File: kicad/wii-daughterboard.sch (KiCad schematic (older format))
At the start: 34 parts, among them J1 Data, J10 USB, J11 A/V Out, J12 Bluetooth Sync, J14 Case Panel, J2 DC In, J3 GameCube 1, J4 GameCube 2, J5 Bluetooth, J6 GameCube 3, J7 GameCube 4, J8 Motherboard Out, U1 TLV62585DRL, U2 TLV62585DRL, U3 TLV62585DRL, U4 MIC94053YC6-TR

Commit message: v2.0
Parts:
- removed J7: GameCube 4, Connector_JST:JST_SH_BM04B-SRSS-TB_1x04-1MP_P1.00mm_Vertical, symbol Connector_Generic_MountingPin:Conn_01x04_MountingPin
- removed U4: MIC94053YC6-TR, Package_TO_SOT_SMD:SOT-363_SC-70-6_Handsoldering, symbol MIC94053:MIC94053YC6-TR
- added J12: Fan Pwr, Connector_JST:JST_SH_BM02B-SRSS-TB_1x02-1MP_P1.00mm_Vertical, symbol Connector:Conn_01x02_Male
- added Q1: DMG2301L, Package_TO_SOT_SMD:SOT-23_Handsoldering, symbol Transistor_FET:DMG2301L
- added R1: 10K, Resistor_SMD:R_0603_1608Metric_Pad1.05x0.95mm_HandSolder, symbol Device:R
- added TP1: 5V, TestPoint:TestPoint_Pad_D1.0mm, symbol Connector:TestPoint
- added TP2: 3V3, TestPoint:TestPoint_Pad_D1.0mm, symbol Connector:TestPoint
- added TP3: 1V15, TestPoint:TestPoint_Pad_D1.0mm, symbol Connector:TestPoint
- added TP4: 1V0, TestPoint:TestPoint_Pad_D1.0mm, symbol Connector:TestPoint
- J10: renamed from J11; value A/V Out -> A/V Pwr
- J11: renamed from J12; value Bluetooth Sync -> BT Sync
- J3: value GameCube 1 -> WaveBird 1; footprint Connector_JST:JST_SH_BM04B-SRSS-TB_1x04-1MP_P1.00mm_Vertical -> Connector_JST:JST_SH_BM03B-SRSS-TB_1x03-1MP_P1.00mm_Vertical; symbol Connector_Generic_MountingPin:Conn_01x04_MountingPin -> Connector_Generic_MountingPin:Conn_01x03_MountingPin
- J4: value GameCube 2 -> WaveBird 2; footprint Connector_JST:JST_SH_BM04B-SRSS-TB_1x04-1MP_P1.00mm_Vertical -> Connector_JST:JST_SH_BM03B-SRSS-TB_1x03-1MP_P1.00mm_Vertical; symbol Connector_Generic_MountingPin:Conn_01x04_MountingPin -> Connector_Generic_MountingPin:Conn_01x03_MountingPin
- J6: value GameCube 3 -> GC 3/4; footprint Connector_JST:JST_SH_BM04B-SRSS-TB_1x04-1MP_P1.00mm_Vertical -> Connector_JST:JST_SH_BM05B-SRSS-TB_1x05-1MP_P1.00mm_Vertical; symbol Connector_Generic_MountingPin:Conn_01x04_MountingPin -> Connector_Generic_MountingPin:Conn_01x05_MountingPin
- J7: renamed from J8; value Motherboard Out -> Mobo Pwr
- J9: renamed from J14; value Case Panel -> Fr. Panel
- renumbered J10 to J8, R1 to R2, R2 to R3, R3 to R4, R4 to R5, R5 to R6, R6 to R7, R7 to R8
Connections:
- net labels added: LED_PWR
- wire segments 194 -> 185
- no-connect marks 7 -> 12
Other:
- note added: "Data"
- note added: "Front Panel"
- note added: "Power Headers"
- note added: "Power Supply"
- note added: "Test Points"
- note removed: "Case Panel"
- note removed: "DC/DC Regulators"
- note removed: "Data Input"
- note removed: "Power Input"
- note removed: "Power Output"
- note removed: "Power Switching"
- moved on the sheet: C1, C2, C3, C4, C5, C6, H1, H2, J10, J2, J7, J8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

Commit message: Fix mosfet bug
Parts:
- R4: value 92K -> 91K
- R8: value 100R -> 150R
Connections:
- net +5V: now also Q1.3 (D); no longer Q1.2 (S)
- net ON_OFF: now also R1.1; no longer R1.2
- net VBUS: now also Q1.2 (S), R1.2; no longer Q1.3 (D), R1.1
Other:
- moved on the sheet: Q1, R1
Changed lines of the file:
@@
-$Comp
-L Device:R R?
-U 1 1 5E85B7C8
-P 4400 4500
-AR Path="/5E83AEBA/5E85B7C8" Ref="R?"  Part="1"
-AR Path="/5E85B7C8" Ref="R4"  Part="1"
-F 0 "R4" H 4470 4546 50  0000 L CNN
-F 1 "92K" H 4470 4455 50  0000 L CNN
-F 2 "Resistor_SMD:R_0603_1608Metric_Pad1.05x0.95mm_HandSolder" V 4330 4500 50  0001 C CNN
-F 3 "~" H 4400 4500 50  0001 C CNN
-	1    4400 4500
-	1    0    0    -1
-$EndComp
 $Comp
 L Device:R R?
@@
 	2300 6150 3000 6150
 Wire Wire Line
-	4700 1900 4700 1300
-Wire Wire Line
-	4150 1900 4700 1900
-Wire Wire Line
-	4150 1850 4150 1900
+	4700 1750 4700 1300
+Wire Wire Line
+	4150 1750 4700 1750
+Wire Wire Line
+	4150 1700 4150 1750
 $Comp
 L power:+5V #PWR014
 U 1 1 5E91E369
+P 4150 1200
+F 0 "#PWR014" H 4150 1050 50  0001 C CNN
+F 1 "+5V" H 4165 1373 50  0000 C CNN
+F 2 "" H 4150 1200 50  0001 C CNN
+F 3 "" H 4150 1200 50  0001 C CNN
+	1    4150 1200
+	1    0    0    -1
+$EndComp
+Wire Wire Line
+	3650 1500 3850 1500
+Connection ~ 3650 1500
+$Comp
+L Device:R R1
+U 1 1 5E8C935F
+P 3650 1850
+F 0 "R1" H 3720 1896 50  0000 L CNN
+F 1 "10K" H 3720 1805 50  0000 L CNN
+F 2 "Resistor_SMD:R_0603_1608Metric_Pad1.05x0.95mm_HandSolder" V 3580 1850 50  0001 C CNN
+F 3 "~" H 3650 1850 50  0001 C CNN
+	1    3650 1850
+	1    0    0    -1
+$EndComp
+$Comp
+L power:VBUS #PWR013
+U 1 1 5E8BD043
 P 4700 1200
-F 0 "#PWR014" H 4700 1050 50  0001 C CNN
-F 1 "+5V" H 4715 1373 50  0000 C CNN
+F 0 "#PWR013" H 4700 1050 50  0001 C CNN
+F 1 "VBUS" H 4715 1373 50  0000 C CNN
 F 2 "" H 4700 1200 50  0001 C CNN
 F 3 "" H 4700 1200 50  0001 C CNN
@@
 	1    0    0    -1
 $EndComp
-Wire Wire Line
-	4150 1250 4150 1450
-Connection ~ 4150 1250
-Wire Wire Line
-	3650 1250 4150 1250
-Wire Wire Line
-	3650 1300 3650 1250
-Wire Wire Line
-	3650 1600 3650 1650
-Wire Wire Line
-	3650 1650 3850 1650
-Connection ~ 3650 1650
-$Comp
-L Device:R R1
-U 1 1 5E8C935F
-P 3650 1450
-F 0 "R1" H 3720 1496 50  0000 L CNN
-F 1 "10K" H 3720 1405 50  0000 L CNN
-F 2 "Resistor_SMD:R_0603_1608Metric_Pad1.05x0.95mm_HandSolder" V 3580 1450 50  0001 C CNN
-F 3 "~" H 3650 1450 50  0001 C CNN
-	1    3650 1450
-	1    0    0    -1
-$EndComp
-Wire Wire Line
-	4150 1200 4150 1250
-$Comp
-L power:VBUS #PWR013
-U 1 1 5E8BD043
-P 4150 1200
-F 0 "#PWR013" H 4150 1050 50  0001 C CNN
-F 1 "VBUS" H 4165 1373 50  0000 C CNN
-F 2 "" H 4150 1200 50  0001 C CNN
-F 3 "" H 4150 1200 50  0001 C CNN
-	1    4150 1200
-	1    0    0    -1
-$EndComp
 $Comp
 L Transistor_FET:DMG2301L Q1
 U 1 1 5E86C656
-P 4050 1650
-F 0 "Q1" H 4254 1696 50  0000 L CNN
-F 1 "DMG2301L" H 4254 1605 50  0000 L CNN
-F 2 "Package_TO_SOT_SMD:SOT-23_Handsoldering" H 4250 1575 50  0001 L CIN
-F 3 "https://www.diodes.com/assets/Datasheets/DMG2301L.pdf" H 4050 1650 50  0001 L CNN
-	1    4050 1650
+P 4050 1500
+F 0 "Q1" H 4254 1546 50  0000 L CNN
+F 1 "DMG2301L" H 4254 1455 50  0000 L CNN
+F 2 "Package_TO_SOT_SMD:SOT-23_Handsoldering" H 4250 1425 50  0001 L CIN
+F 3 "https://www.diodes.com/assets/Datasheets/DMG2301L.pdf" H 4050 1500 50  0001 L CNN
+	1    4050 1500
 	1    0    0    -1
 $EndComp
@@
 Wire Notes Line
 	5000 550  2050 550
-Text Label 3250 1650 0    50   ~ 0
+Text Label 3250 1500 0    50   ~ 0
 ON_OFF
 Wire Wire Line
-	3250 1650 3650 1650
+	3250 1500 3650 1500
 Wire Notes Line
 	2050 550  2050 7500
@@
 $EndComp
 NoConn ~ 10150 2950
-$Comp
-L Device:R R8
-U 1 1 5F20DF16
-P 9400 2450
-F 0 "R8" V 9193 2450 50  0000 C CNN
-F 1 "100R" V 9284 2450 50  0000 C CNN
-F 2 "Resistor_SMD:R_0603_1608Metric_Pad1.05x0.95mm_HandSolder" V 9330 2450 50  0001 C CNN
-F 3 "~" H 9400 2450 50  0001 C CNN
-	1    9400 2450
-	0    1    1    0
-$EndComp
 Wire Wire Line
 	9550 2450 9950 2450
@@
 Text Notes 10900 5650 2    50   ~ 0
 Test Points
+$Comp
+L Device:R R8
+U 1 1 5F20DF16
+P 9400 2450
+F 0 "R8" V 9193 2450 50  0000 C CNN
+F 1 "150R" V 9284 2450 50  0000 C CNN
+F 2 "Resistor_SMD:R_0603_1608Metric_Pad1.05x0.95mm_HandSolder" V 9330 2450 50  0001 C CNN
+F 3 "~" H 9400 2450 50  0001 C CNN
+	1    9400 2450
+	0    1    1    0
+$EndComp
+$Comp
+L Device:R R?
+U 1 1 5E85B7C8
+P 4400 4500
+AR Path="/5E83AEBA/5E85B7C8" Ref="R?"  Part="1"
+AR Path="/5E85B7C8" Ref="R4"  Part="1"
+F 0 "R4" H 4470 4546 50  0000 L CNN
+F 1 "91K" H 4470 4455 50  0000 L CNN
+F 2 "Resistor_SMD:R_0603_1608Metric_Pad1.05x0.95mm_HandSolder" V 4330 4500 50  0001 C CNN
+F 3 "~" H 4400 4500 50  0001 C CNN
+	1    4400 4500
+	1    0    0    -1
+$EndComp
+Wire Wire Line
+	3650 1500 3650 1700
+Wire Wire Line
+	4150 1200 4150 1300
+Connection ~ 4700 1750
+Wire Wire Line
+	4700 2000 4700 1750
+Wire Wire Line
+	3650 2000 4700 2000
 $EndSCHEMATC

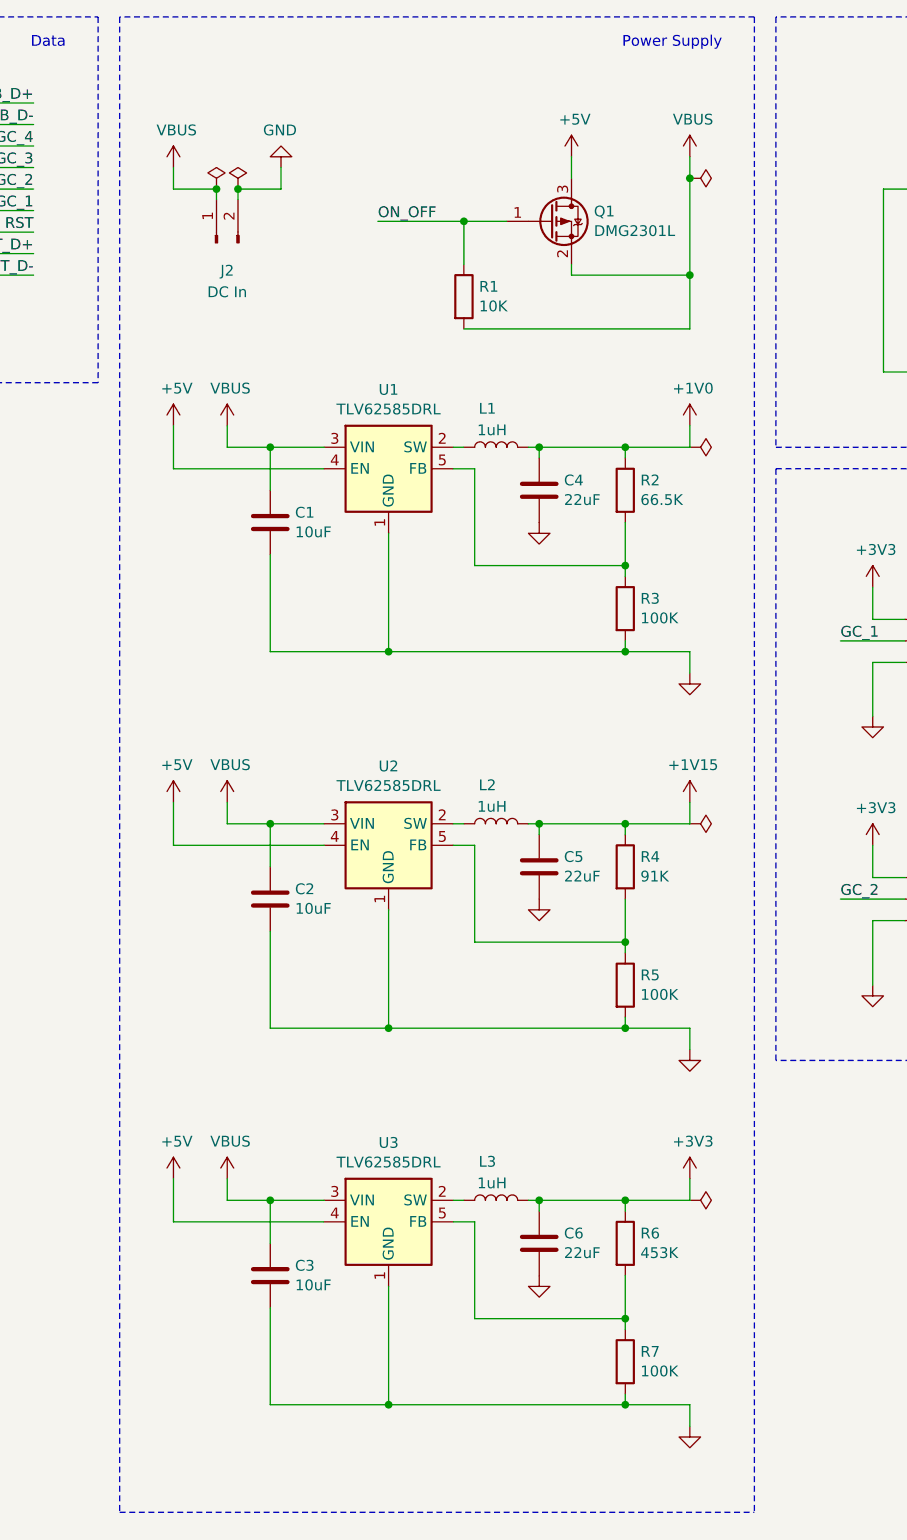
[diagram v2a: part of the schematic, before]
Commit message: Fix MOSFET orientation, add pulldown
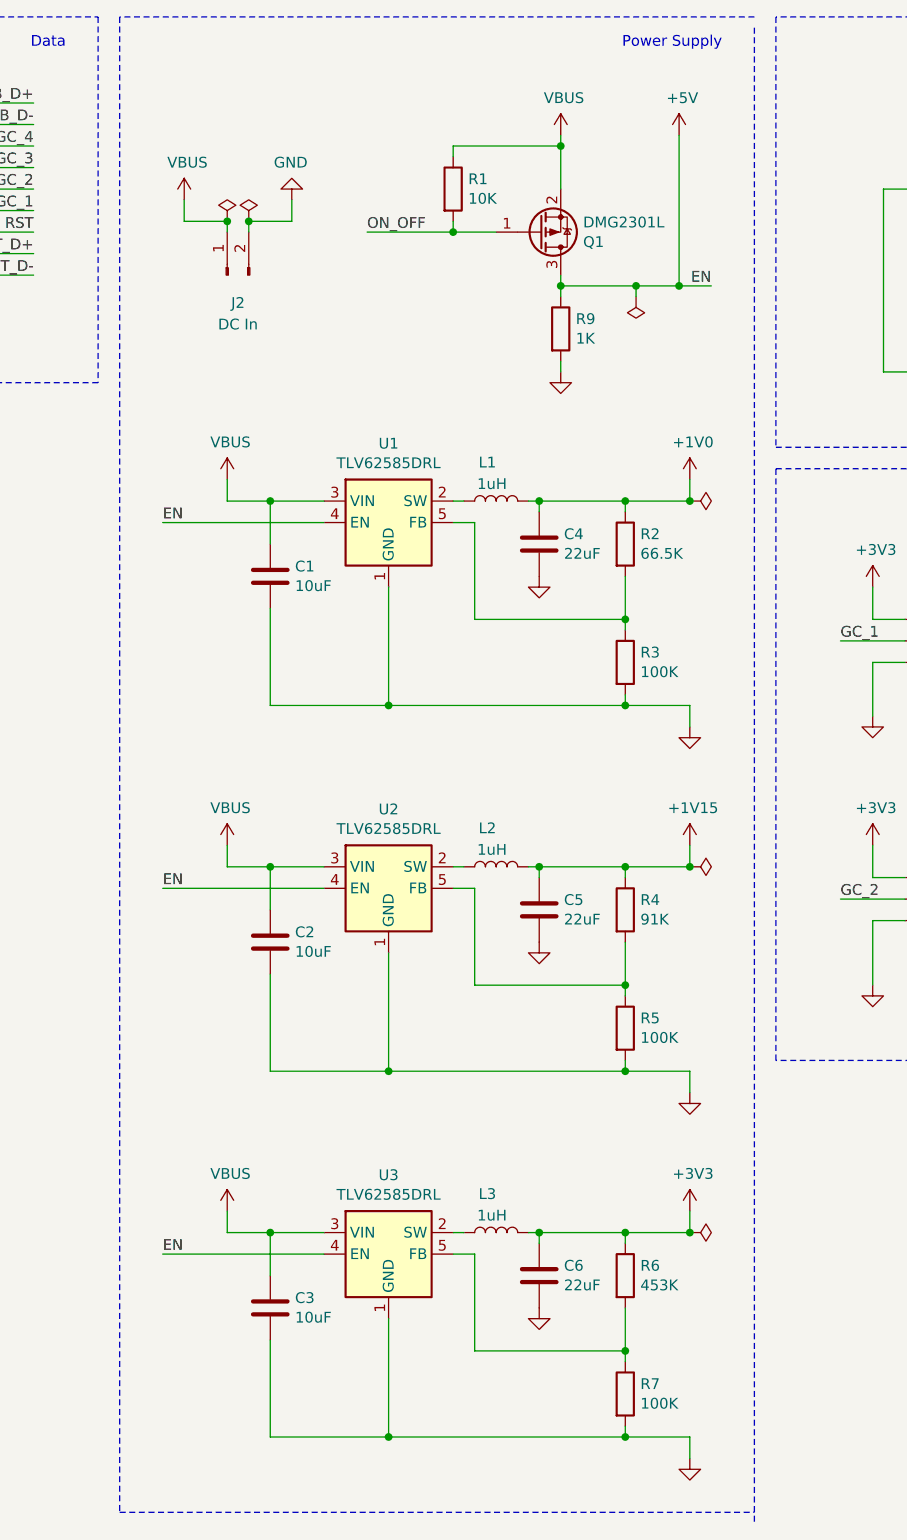
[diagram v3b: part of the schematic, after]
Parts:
- added R9: 1K, symbol Device:R
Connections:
- net +5V: now also R9.1
- net GND: now also R9.2
- net ON_OFF: now also R1.2; no longer R1.1
- net VBUS: now also R1.1; no longer R1.2
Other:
- moved on the sheet: C1, C2, C3, C4, C5, C6, J2, L1, L2, L3, Q1, R1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
